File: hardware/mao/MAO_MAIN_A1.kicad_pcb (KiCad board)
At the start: 4 copper layers, 58 x 56 mm, 142 parts, among them J101 USB-C, J102 BAT, J201 TAG, J301 LCD, J501 LRA, Q101 AO3401A, Q102 2N7002, Q302 DMG2302UKQ, Q501 AO3400A, SW301 SKQGAFE010, SW302 SKQGAFE010, SW303 SKQGAFE010, U101 TPD2E2U06, U102 BQ25185DLHR, U103 MAX17048G+T10, U104 TPS62840DLCR, U105 TPS22916CYFPR, U201 ESP32-S3-MINI-1-N8, U301 DRV5012AEDMRR, U302 DRV5012AEDMRR, U304 TLV9061IDBVR, U401 ICM-42670-P, U402 VL53L4CDV0DH/1, U501 MAX98357AETE+T, U502 DRV2605LDGST, U503 IRM-H638T/TR2, U504 TPS22916CYFPR

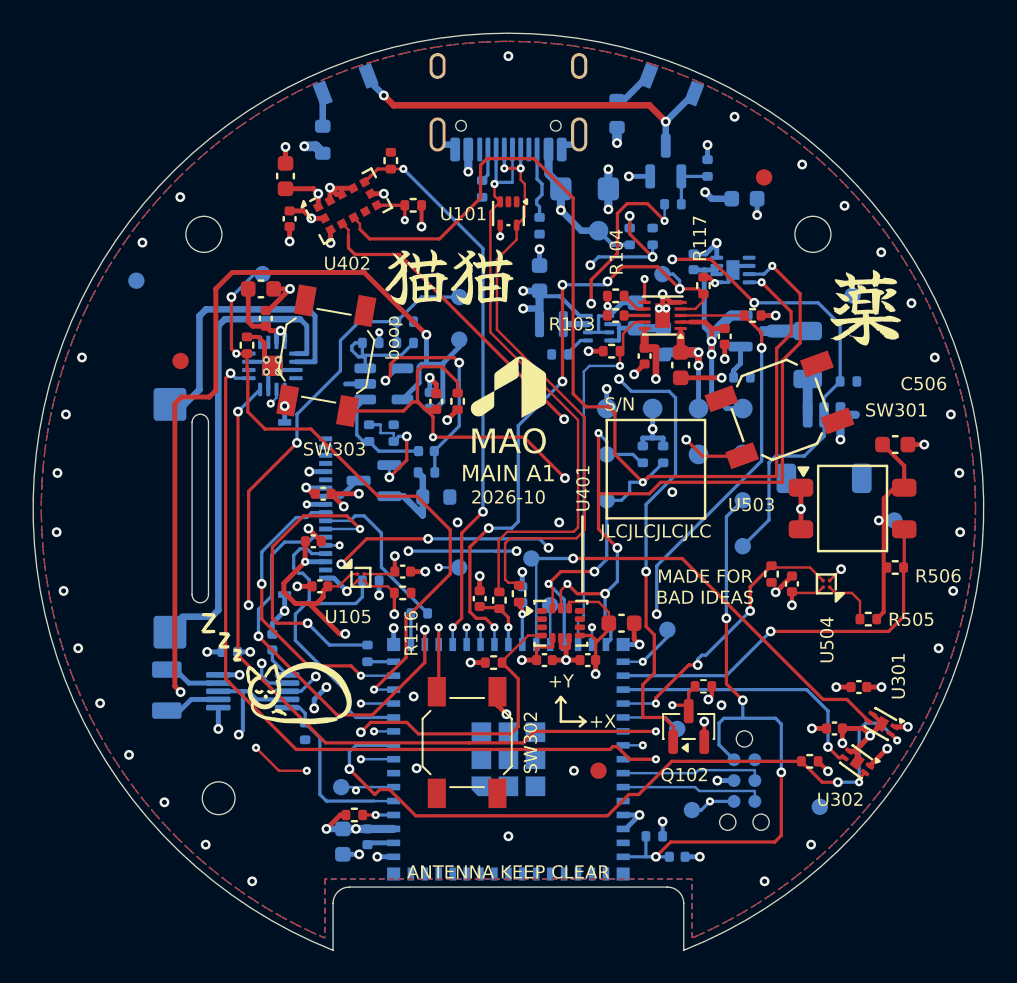
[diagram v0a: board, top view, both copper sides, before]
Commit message: A1 face press: an even switch triangle; the display tail's well shortened
Owner decision 2026-10-07: the three face switches as a neat triangle
pointing at the centre, the display ribbon kept clear of them (it keeps
its 9 o'clock exit, slot and J301).

- Switches at 85 / 205 / 325 deg, r 13.5 / 14.25 / 13.5, square-on to the
  centre (SW302 turned 90 deg on its centre, same body, and 0.75 mm out so
  its keep-out misses the module's pin 12-14 escape vias). Centre press
  shares 34 / 32 / 34 % (was 29 / 35.5 / 35.5).
- A sweep over every rotation, radius and turn found no even triangle on
  the board as it was; the family near 85 deg fits once the tail well is
  shortened from x 6..12 to x 5.6..9.9 (0.34 mm to SW301).
- Copper (route_triangle.py, recorded): the displaced copper is ripped
  and grid-routed. PRESS_N to SW302, AMP_SD (with LCD_TE lifted out of
  its way) and LCD_TE (4 vias) were hand-drawn after a free-space search
  confirmed each route. The +3V3 feed of the panel rail switch drops to
  the main L3 plane, with a small L3 no-pour pocket so the plane stays
  one piece. One GND stitching via was removed for the S/N field.
- Silk: the S/N field's inside must hold no other silk (it had framed
  the identity block); the field moved to (7.2, -2.4) and JLC's
  order-number placeholder takes its own nearest clear spot.
- Wheel stone: bosses on the new switch spots and the shorter well; the
  clash check still finds 0; the carrier STL is re-exported.

Checks: DRC 0 violations / 0 unconnected, planes one piece each,
mech_check 0, silk text 0, wheel-stone clash 0. Fab package, renders,
egg close-ups and a triangle / ribbon overlay are regenerated.

Co-Authored-By: Claude Opus 5.5 <noreply@anthropic.com>
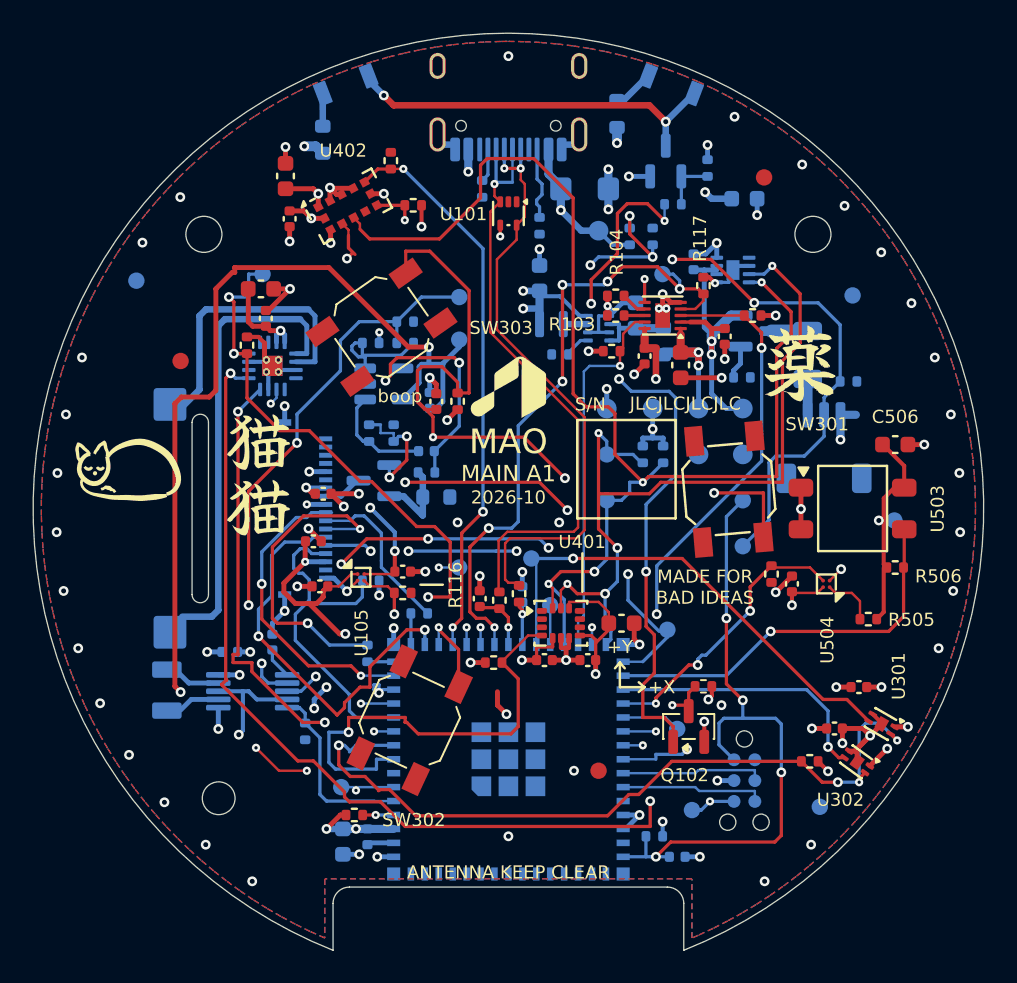
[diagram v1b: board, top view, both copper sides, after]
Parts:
- moved SW301 5.74 mm to (63.4, 48.8), turned to -85 degrees
- moved SW303 3.79 mm to (42.3, 38.9), turned to 35 degrees
- moved SW302 3.76 mm to (44.0, 62.9), turned to -115 degrees
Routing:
- net PRESS_N: track 52.5 -> 67.3 mm
- net AMP_DIN: track 50.4 -> 61.5 mm, vias 2 -> 3
- net LCD_TE: track 28.7 -> 35.3 mm, vias 2 -> 4
- net IMU_INT1: track 21.7 -> 28.0 mm, vias 2 -> 1
- net AMP_SD: track 39.3 -> 43.4 mm, vias 3 -> 4
- net +3V3: track 54.0 -> 57.6 mm, vias 27 -> 28
- net AMP_BCLK: track 46.8 -> 49.3 mm, vias 2 -> 3
- net HALL_FAST: track 45.8 -> 47.3 mm
- net I2C_SCL: track 102.7 -> 102.1 mm
- net GND: vias 92 -> 89

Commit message: A1 press: P3, the whole top presses one switch on the back (owner decision 2026-10-07)
The face tripod (three SKQGAFE010 on F) gives way to P3: wheel, bezel, window,
panel, carrier, frame and the board slide 0.45 mm on the base; one ALPS
SKQGADE010 (C116647) on B.Cu at (8.0, 3.8) meets a 1.5 mm stainless finger
fixed to the base, reaching over the cell from 12 o'clock.

Board: SW302/SW303 removed, SW301 to B, TP19 steps 0.45 mm, the tail well
back to x 6..12; route_press3.py records the place/well/rip/escape/add steps
(CHG_STAT1/2, I2C_SCL, HALL_A and LCD_TE re-drawn by hand after a free-space
search). Silk re-placed (boop on B, S/N field empty inside). ERC 0, DRC 0 /
0 unconnected / 0 parity, planes one piece, mech 0, silk 0, stack-up
broadside 16.8 mm, fab BOM 49 lines / 100 parts.

Enclosure: guide columns with brass spacers in the base (the hard stop),
the frame wall slotted round them, snap ledges and pins for the board, the
finger and its root posts, carrier feet; clash check 0 at rest and pressed.
Finger STL (fit) and DXF (laser cut); sections, renders, plots, docs.

Co-Authored-By: Claude Opus 5.5 <noreply@anthropic.com>
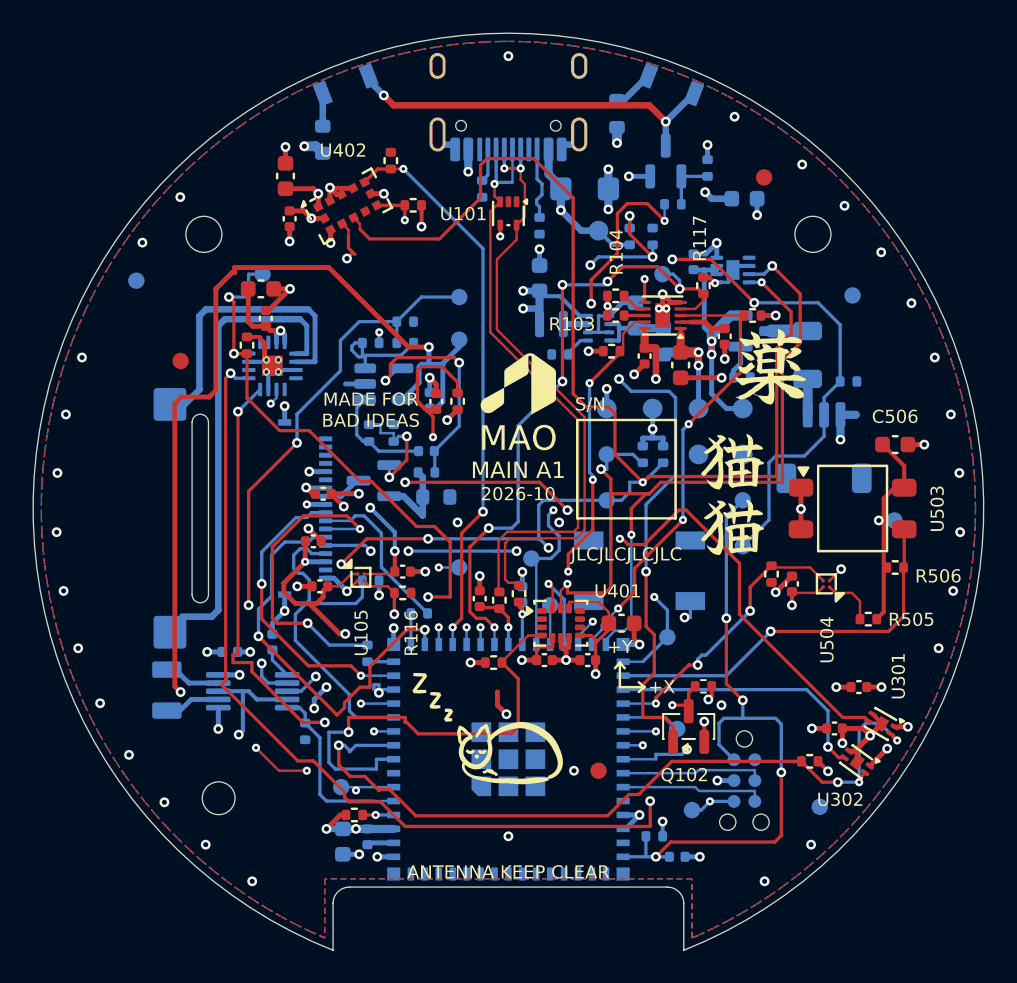
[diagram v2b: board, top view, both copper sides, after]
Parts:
- removed SW302, SW303: SKQGAFE010, Button_Switch_SMD:SW_SPST_SKQG_WithStem
- SW301: value SKQGAFE010 -> SKQGADE010; moved to B.Cu
- moved SW301 7.38 mm to (58.0, 53.8), turned to 0 degrees
- moved TP19 0.45 mm to (59.7, 57.9)
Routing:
- net PRESS_N: track 67.3 -> 43.6 mm, vias 5 -> 4
- net HALL_A: track 30.1 -> 38.8 mm, vias 1 -> 2
- net I2C_SCL: track 102.1 -> 106.1 mm, vias 9 -> 8
- net CHG_STAT2: track 30.8 -> 27.7 mm
- net I2C_SDA: track 104.5 -> 103.0 mm, vias 8 -> 7
- net LCD_TE: track 35.3 -> 36.3 mm
- net CHG_STAT1: track 22.8 -> 23.0 mm, vias 1 -> 4
